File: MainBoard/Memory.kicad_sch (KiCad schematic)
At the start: 9 parts, among them U2 74AHCT04, U66 ATF22V10C, U67 CD74HC173PWR

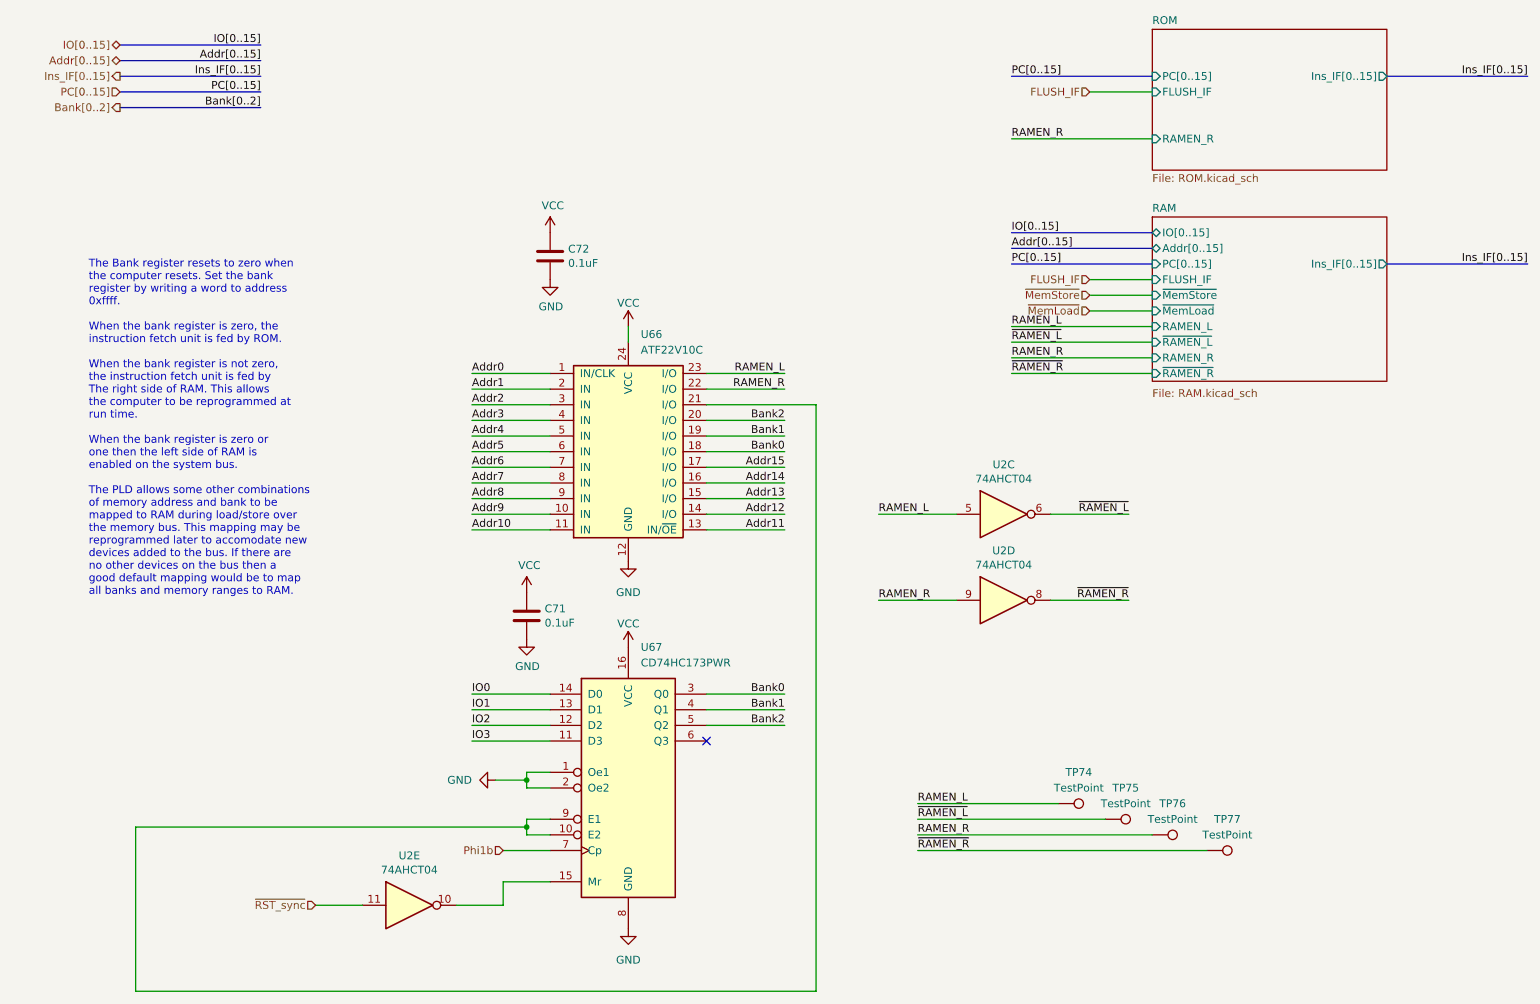
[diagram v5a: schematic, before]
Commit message: MainBoard: incorporate changes to MEM unit bank register
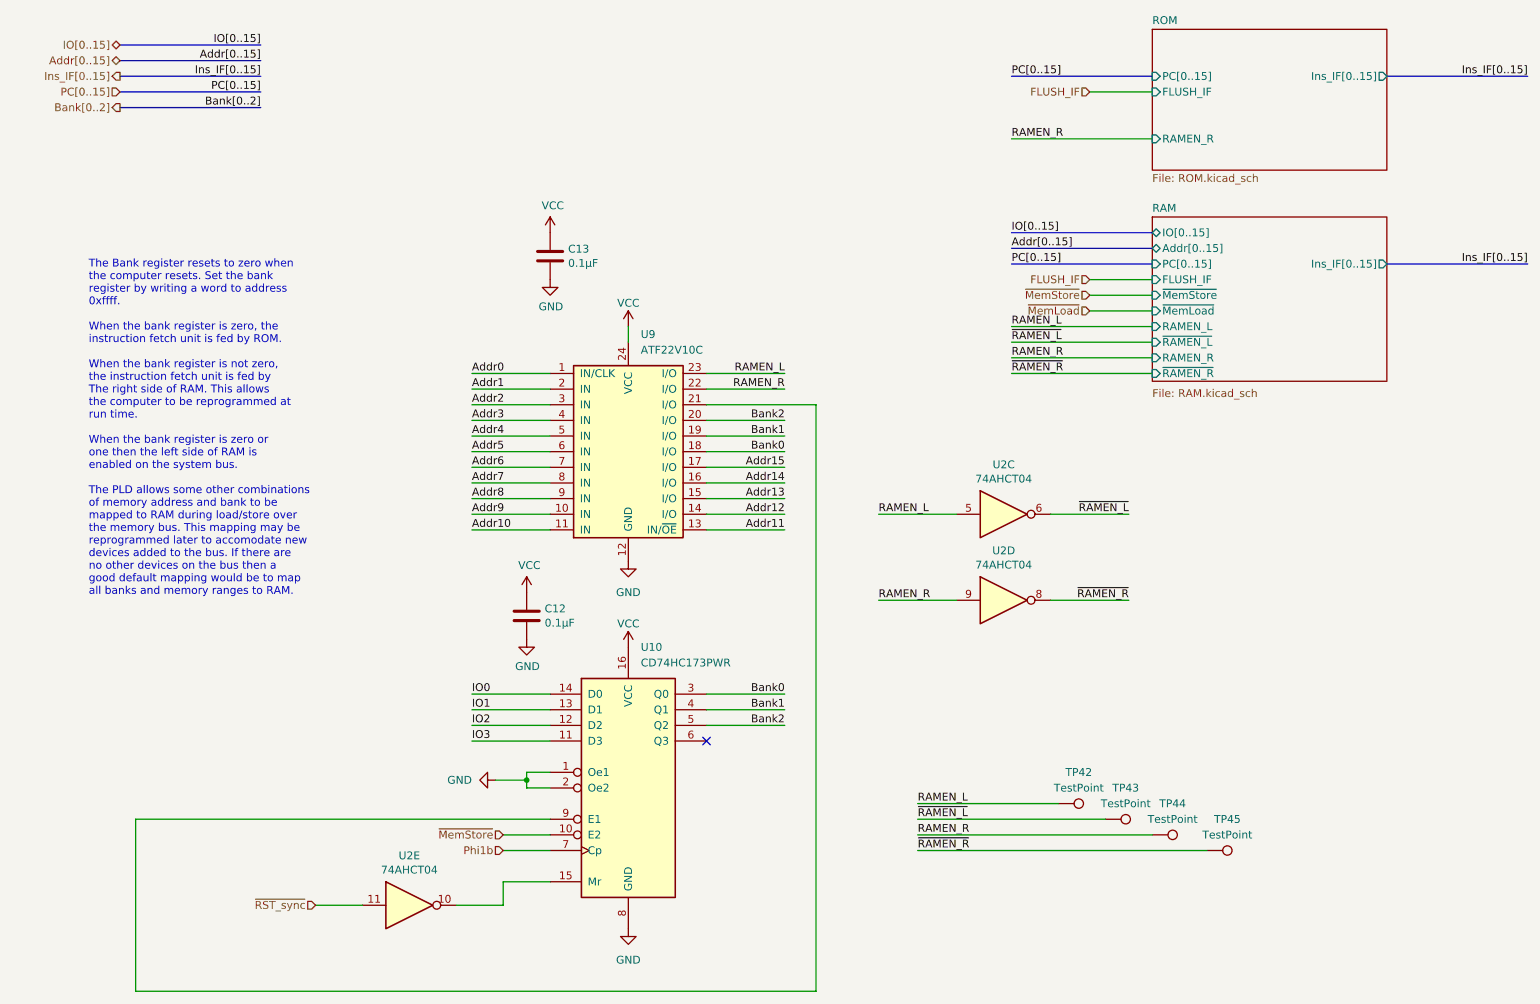
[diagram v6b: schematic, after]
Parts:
- C12: renamed from C71; value 0.1uF -> 0.1μF
- C13: renamed from C72; value 0.1uF -> 0.1μF
- renumbered TP74 to TP42, TP75 to TP43, TP76 to TP44, TP77 to TP45, U67 to U10, U66 to U9
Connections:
- net ~{MemStore}: now also U10.10 (E2)
- net at U10.9 (E1), U9.21 (I/O): no longer U10.10 (E2)
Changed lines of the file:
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@@
   (paper "A4")
   (title_block
-    (date "2023-10-22")
-    (rev "C")
+    (date "2023-10-28")
+    (rev "D")
   )
   (junction (at 104.14 144.78) (diameter 0) (color 0 0 0 0)
-  )
-  (junction (at 104.14 152.4) (diameter 0) (color 0 0 0 0)
   )
   (no_connect (at 133.35 138.43))
@@
     (stroke (width 0) (type default))
   )
-  (wire (pts (xy 104.14 152.4) (xy 40.64 152.4))
-    (stroke (width 0) (type default))
-  )
   (bus (pts (xy 38.1 33.02) (xy 60.96 33.02))
     (stroke (width 0) (type default))
@@
     (stroke (width 0) (type default))
   )
-  (wire (pts (xy 107.95 151.13) (xy 104.14 151.13))
+  (wire (pts (xy 40.64 151.13) (xy 107.95 151.13))
     (stroke (width 0) (type default))
   )
@@
     (stroke (width 0) (type default))
   )
-  (wire (pts (xy 104.14 153.67) (xy 107.95 153.67))
-    (stroke (width 0) (type default))
-  )
   (wire (pts (xy 95.25 91.44) (xy 107.95 91.44))
     (stroke (width 0) (type default))
@@
     (stroke (width 0) (type default))
   )
-  (wire (pts (xy 40.64 152.4) (xy 40.64 179.07))
+  (wire (pts (xy 40.64 151.13) (xy 40.64 179.07))
     (stroke (width 0) (type default))
   )
@@
     (stroke (width 0) (type default))
   )
-  (wire (pts (xy 104.14 151.13) (xy 104.14 152.4))
-    (stroke (width 0) (type default))
-  )
   (wire (pts (xy 104.14 146.05) (xy 107.95 146.05))
     (stroke (width 0) (type default))
@@
     (stroke (width 0) (type default))
   )
+  (wire (pts (xy 100.33 153.67) (xy 107.95 153.67))
+    (stroke (width 0) (type default))
+  )
   (wire (pts (xy 95.25 96.52) (xy 107.95 96.52))
     (stroke (width 0) (type default))
@@
   )
   (wire (pts (xy 167.64 153.67) (xy 205.74 153.67))
-    (stroke (width 0) (type default))
-  )
-  (wire (pts (xy 104.14 152.4) (xy 104.14 153.67))
     (stroke (width 0) (type default))
   )
@@
     (effects (font (size 1.27 1.27)) (justify right))
   )
+  (hierarchical_label "~{MemStore}" (shape input) (at 100.33 153.67 180) (fields_autoplaced)
+    (effects (font (size 1.27 1.27)) (justify right))
+  )
   (hierarchical_label "IO[0..15]" (shape tri_state) (at 38.1 25.4 180) (fields_autoplaced)
     (effects (font (size 1.27 1.27)) (justify right))
@@
   (symbol (lib_id "MEMModule-rescue:ATF22V10C-Logic_Programmable") (at 120.65 90.17 0) (unit 1)
     (in_bom yes) (on_board yes) (dnp no) (fields_autoplaced)
-    (property "Reference" "U66" (at 122.6694 72.39 0)
+    (property "Reference" "U9" (at 122.6694 72.39 0)
       (effects (font (size 1.27 1.27)) (justify left))
     )
@@
   (symbol (lib_id "power:GND") (at 104.14 121.92 0) (unit 1)
     (in_bom yes) (on_board yes) (dnp no)
-    (property "Reference" "#PWR0398" (at 104.14 128.27 0)
+    (property "Reference" "#PWR0141" (at 104.14 128.27 0)
       (effects (font (size 1.27 1.27)) hide)
     )
@@
   (symbol (lib_id "power:GND") (at 99.06 144.78 270) (unit 1)
     (in_bom yes) (on_board yes) (dnp no) (fields_autoplaced)
-    (property "Reference" "#PWR0396" (at 92.71 144.78 0)
+    (property "Reference" "#PWR0139" (at 92.71 144.78 0)
       (effects (font (size 1.27 1.27)) hide)
     )
@@
   (symbol (lib_id "Device:C") (at 107.95 59.69 0) (unit 1)
     (in_bom yes) (on_board yes) (dnp no)
-    (property "Reference" "C72" (at 110.871 58.5216 0)
+    (property "Reference" "C13" (at 110.871 58.5216 0)
       (effects (font (size 1.27 1.27)) (justify left))
     )
-    (property "Value" "0.1uF" (at 110.871 60.833 0)
+    (property "Value" "0.1μF" (at 110.871 60.833 0)
       (effects (font (size 1.27 1.27)) (justify left))
     )
@@
   (symbol (lib_id "Device:C") (at 104.14 118.11 0) (unit 1)
     (in_bom yes) (on_board yes) (dnp no)
-    (property "Reference" "C71" (at 107.061 116.9416 0)
+    (property "Reference" "C12" (at 107.061 116.9416 0)
       (effects (font (size 1.27 1.27)) (justify left))
     )
-    (property "Value" "0.1uF" (at 107.061 119.253 0)
+    (property "Value" "0.1μF" (at 107.061 119.253 0)
       (effects (font (size 1.27 1.27)) (justify left))
     )
@@
   (symbol (lib_id "Connector:TestPoint") (at 214.63 156.21 270) (mirror x) (unit 1)
     (in_bom yes) (on_board yes) (dnp no)
-    (property "Reference" "TP77" (at 217.932 151.13 90)
+    (property "Reference" "TP45" (at 217.932 151.13 90)
       (effects (font (size 1.27 1.27)))
     )
@@
   (symbol (lib_id "power:GND") (at 120.65 168.91 0) (unit 1)
     (in_bom yes) (on_board yes) (dnp no) (fields_autoplaced)
-    (property "Reference" "#PWR0404" (at 120.65 175.26 0)
+    (property "Reference" "#PWR0147" (at 120.65 175.26 0)
       (effects (font (size 1.27 1.27)) hide)
     )
@@
   (symbol (lib_id "power:GND") (at 120.65 109.22 0) (unit 1)
     (in_bom yes) (on_board yes) (dnp no) (fields_autoplaced)
-    (property "Reference" "#PWR0402" (at 120.65 115.57 0)
+    (property "Reference" "#PWR0145" (at 120.65 115.57 0)
       (effects (font (size 1.27 1.27)) hide)
     )
@@
   (symbol (lib_id "74xx:74LS173") (at 120.65 146.05 0) (unit 1)
     (in_bom yes) (on_board yes) (dnp no) (fields_autoplaced)
-    (property "Reference" "U67" (at 122.6694 123.19 0)
+    (property "Reference" "U10" (at 122.6694 123.19 0)
       (effects (font (size 1.27 1.27)) (justify left))
     )
@@
   (symbol (lib_id "Connector:TestPoint") (at 205.74 153.67 270) (mirror x) (unit 1)
     (in_bom yes) (on_board yes) (dnp no)
-    (property "Reference" "TP76" (at 209.042 148.59 90)
+    (property "Reference" "TP44" (at 209.042 148.59 90)
       (effects (font (size 1.27 1.27)))
     )
@@
   (symbol (lib_id "power:VCC") (at 120.65 123.19 0) (unit 1)
     (in_bom yes) (on_board yes) (dnp no)
-    (property "Reference" "#PWR0403" (at 120.65 127 0)
+    (property "Reference" "#PWR0146" (at 120.65 127 0)
       (effects (font (size 1.27 1.27)) hide)
     )
@@
   (symbol (lib_id "power:GND") (at 107.95 63.5 0) (unit 1)
     (in_bom yes) (on_board yes) (dnp no)
-    (property "Reference" "#PWR0400" (at 107.95 69.85 0)
+    (property "Reference" "#PWR0143" (at 107.95 69.85 0)
       (effects (font (size 1.27 1.27)) hide)
     )
@@
   (symbol (lib_id "Connector:TestPoint") (at 190.5 148.59 270) (mirror x) (unit 1)
     (in_bom yes) (on_board yes) (dnp no)
-    (property "Reference" "TP74" (at 193.802 143.51 90)
+    (property "Reference" "TP42" (at 193.802 143.51 90)
       (effects (font (size 1.27 1.27)))
     )
@@
   (symbol (lib_id "power:VCC") (at 104.14 114.3 0) (unit 1)
     (in_bom yes) (on_board yes) (dnp no)
-    (property "Reference" "#PWR0397" (at 104.14 118.11 0)
+    (property "Reference" "#PWR0140" (at 104.14 118.11 0)
       (effects (font (size 1.27 1.27)) hide)
     )
@@
   (symbol (lib_id "power:VCC") (at 107.95 55.88 0) (unit 1)
     (in_bom yes) (on_board yes) (dnp no)
-    (property "Reference" "#PWR0399" (at 107.95 59.69 0)
+    (property "Reference" "#PWR0142" (at 107.95 59.69 0)
       (effects (font (size 1.27 1.27)) hide)
     )
@@
   (symbol (lib_id "Connector:TestPoint") (at 198.12 151.13 270) (mirror x) (unit 1)
     (in_bom yes) (on_board yes) (dnp no)
-    (property "Reference" "TP75" (at 201.422 146.05 90)
+    (property "Reference" "TP43" (at 201.422 146.05 90)
       (effects (font (size 1.27 1.27)))
     )
@@
   (symbol (lib_id "power:VCC") (at 120.65 71.12 0) (unit 1)
     (in_bom yes) (on_board yes) (dnp no)
-    (property "Reference" "#PWR0401" (at 120.65 74.93 0)
+    (property "Reference" "#PWR0144" (at 120.65 74.93 0)
       (effects (font (size 1.27 1.27)) hide)
     )
@@
       (effects (font (size 1.27 1.27)) (justify right))
     )
-  )
+    (instances
+    )
+  )

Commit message: MainBoard: Update schematics and PCB placement for ControlModule changes
This includes the fix for the STALL bug and the control signal ordering
bug. The PCB trace routing has been cleared and is not updated yet.
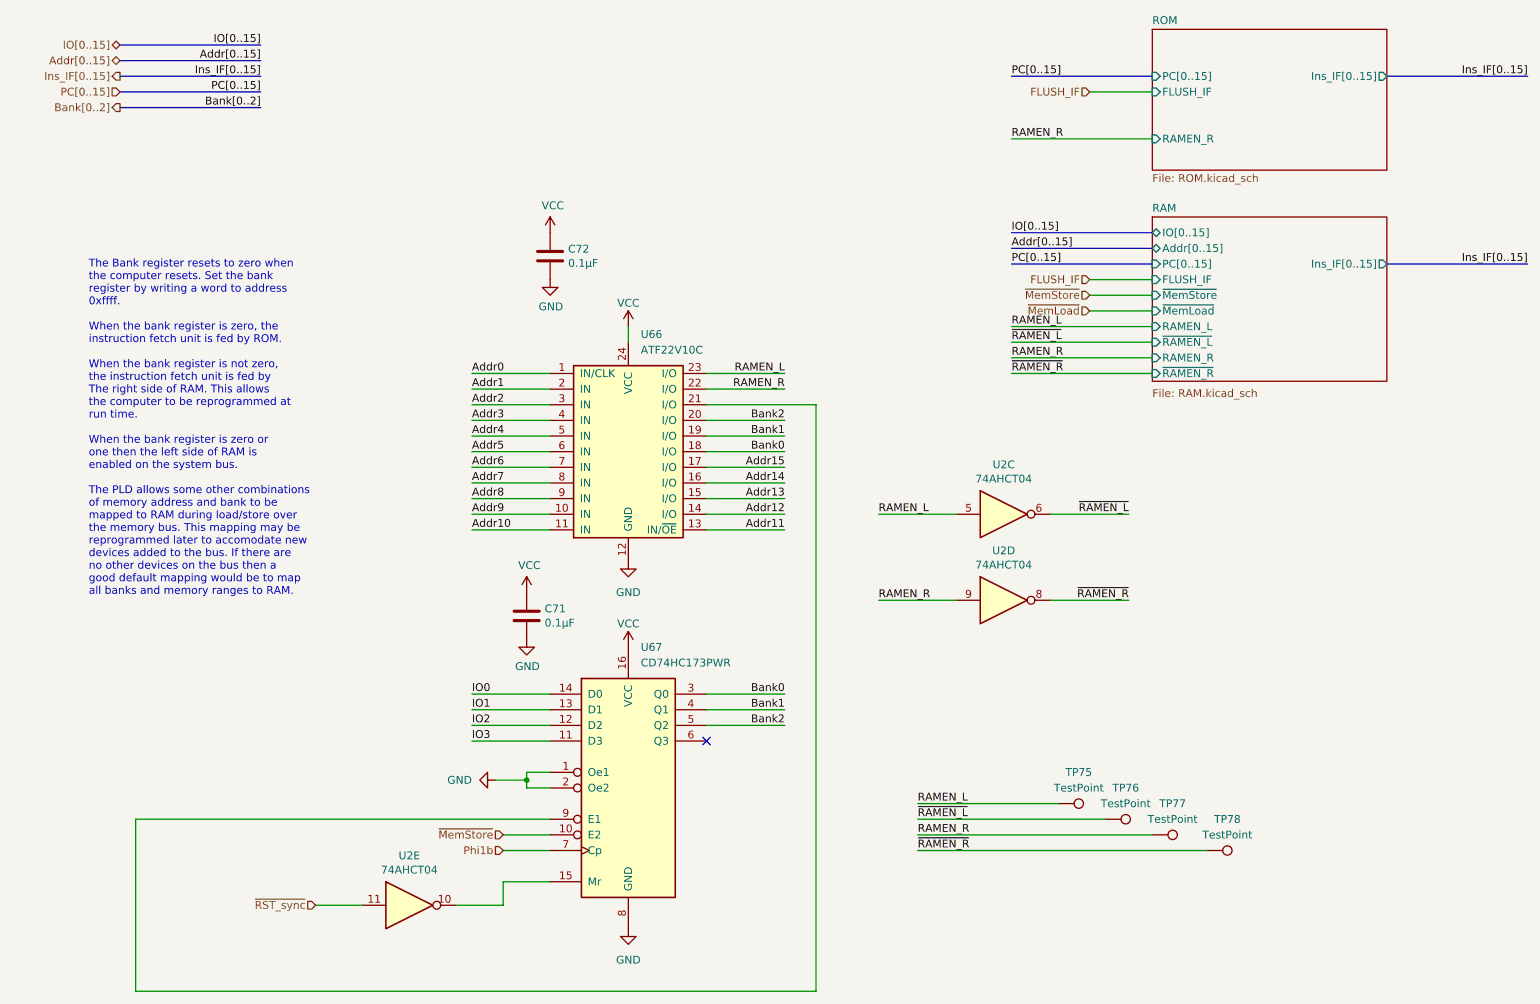
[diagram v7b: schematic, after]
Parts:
- renumbered C12 to C71, C13 to C72, TP42 to TP75, TP43 to TP76, TP44 to TP77, TP45 to TP78, U9 to U66, U10 to U67

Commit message: MainBoard: Update schematics and PCB placement for Register File fix
This includes changes to fix the register file timing issue with the
/WBEN signal.
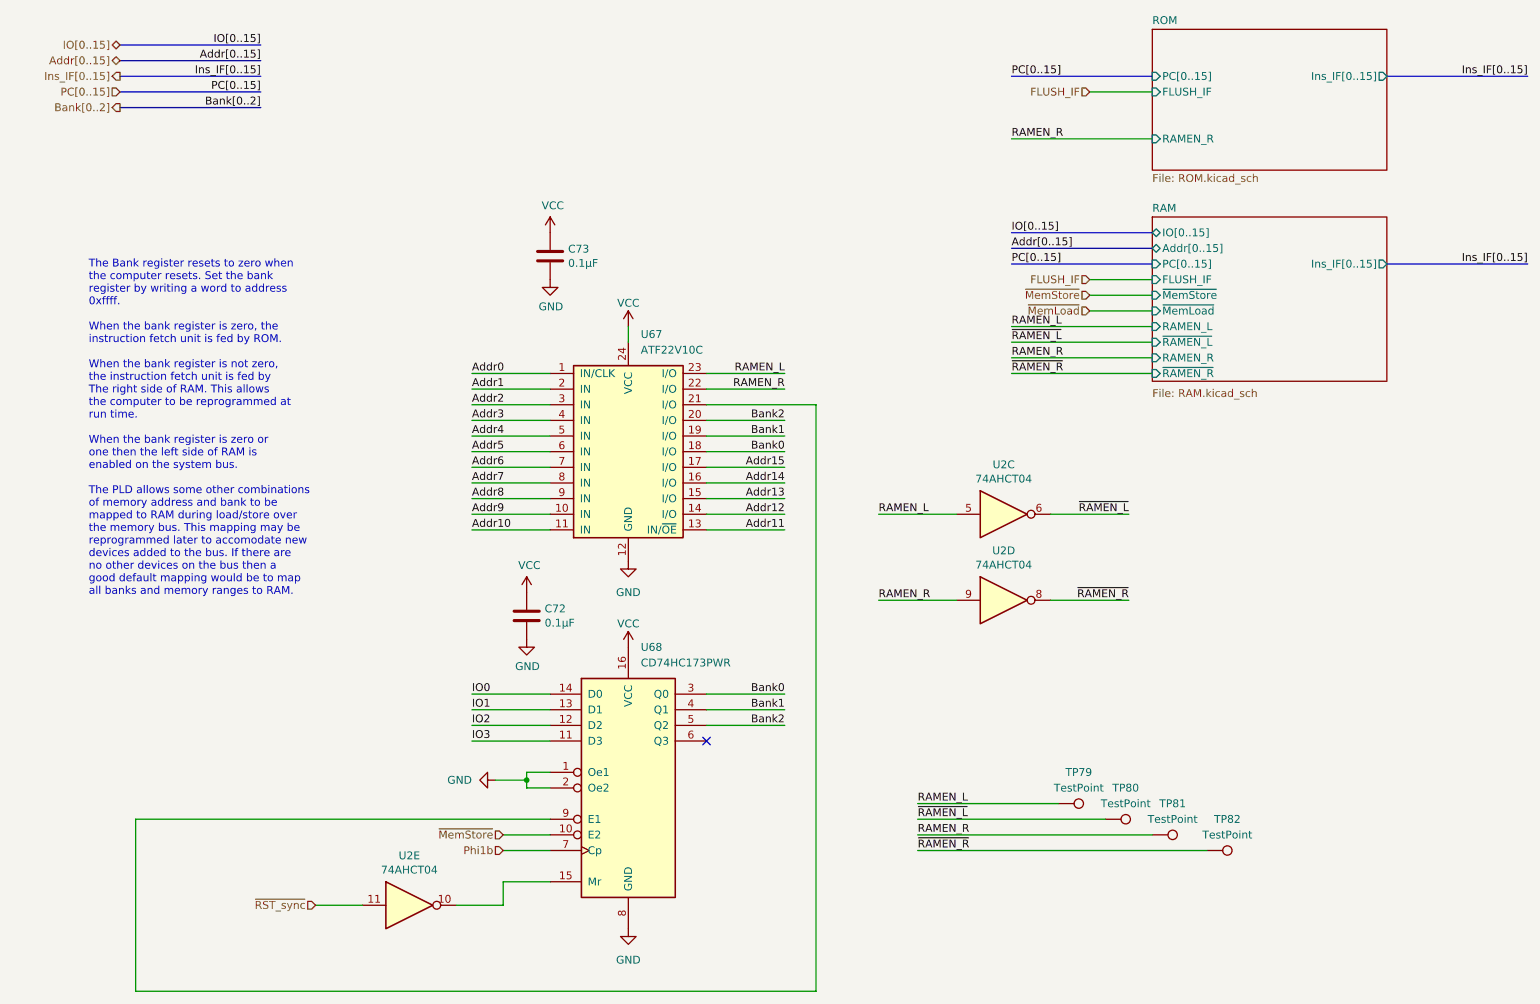
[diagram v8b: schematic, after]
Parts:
- renumbered C71 to C72, C72 to C73, TP75 to TP79, TP76 to TP80, TP77 to TP81, TP78 to TP82, U66 to U67, U67 to U68
